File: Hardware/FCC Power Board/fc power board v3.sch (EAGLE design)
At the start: 40 parts

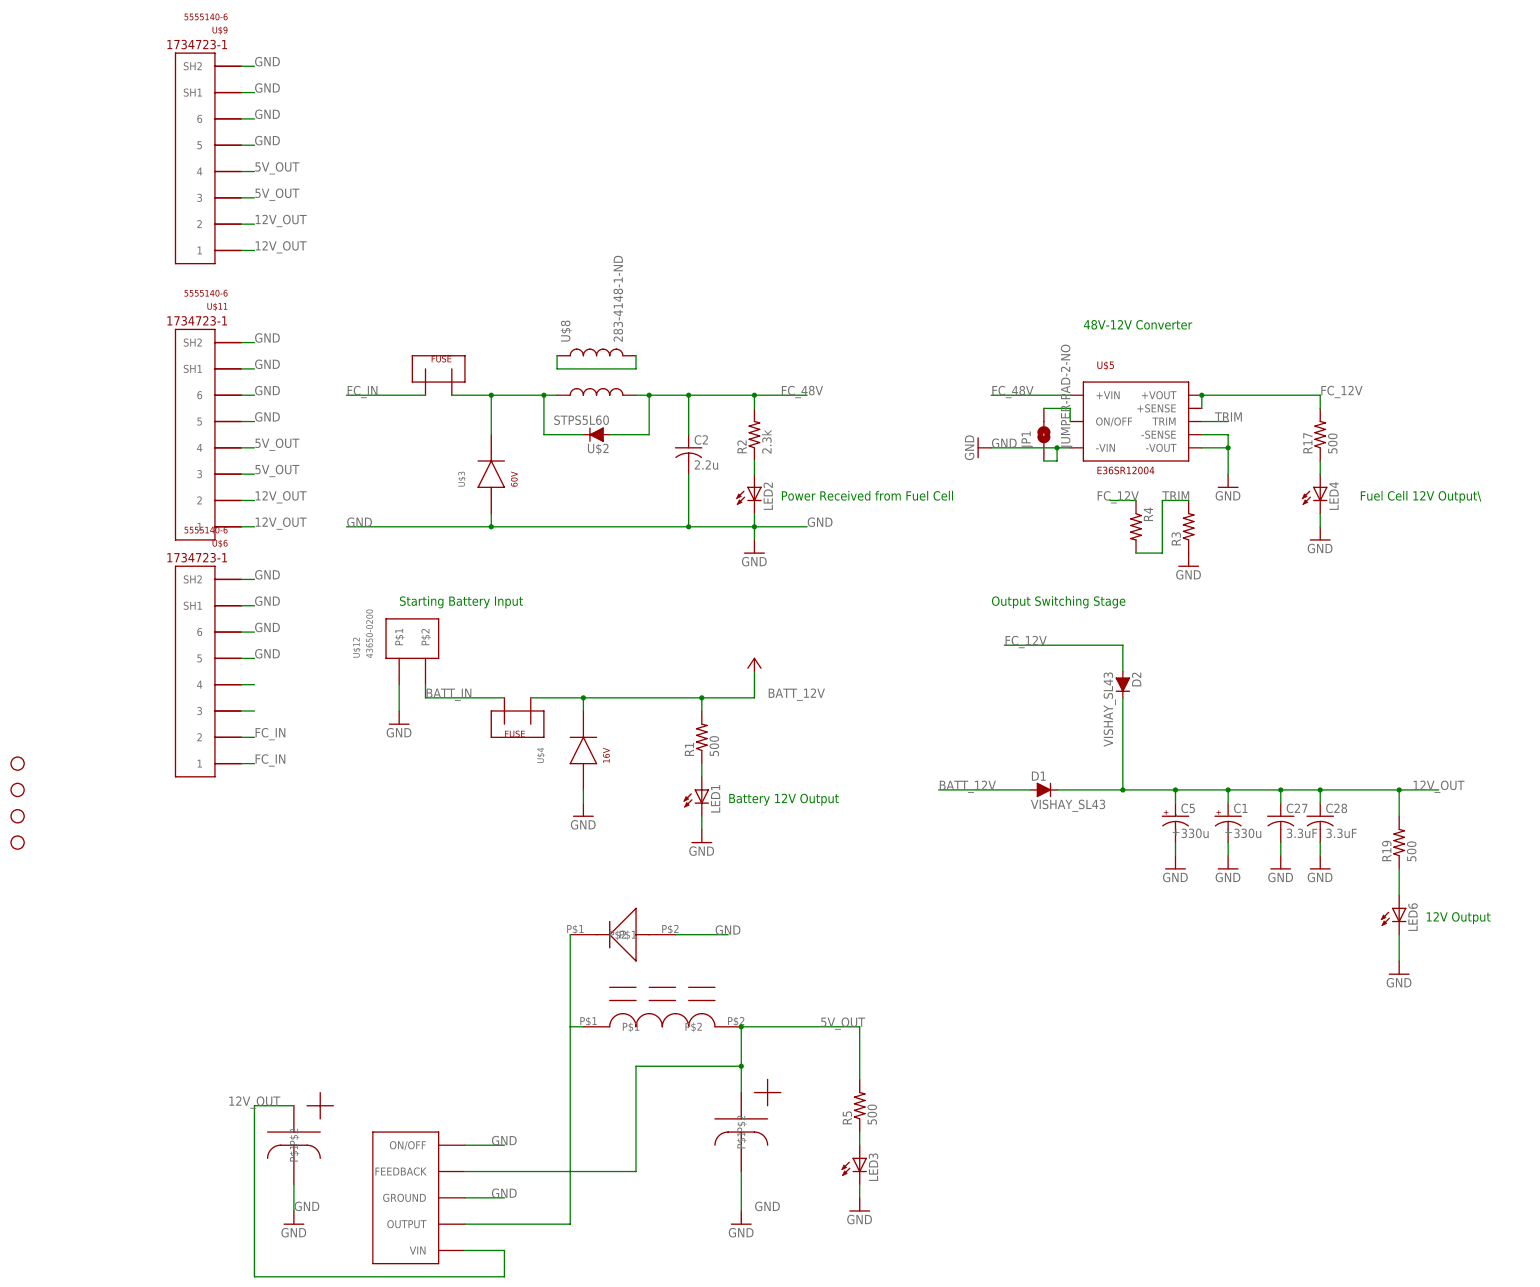
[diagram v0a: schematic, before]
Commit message: cleaned up fc power board silk screen
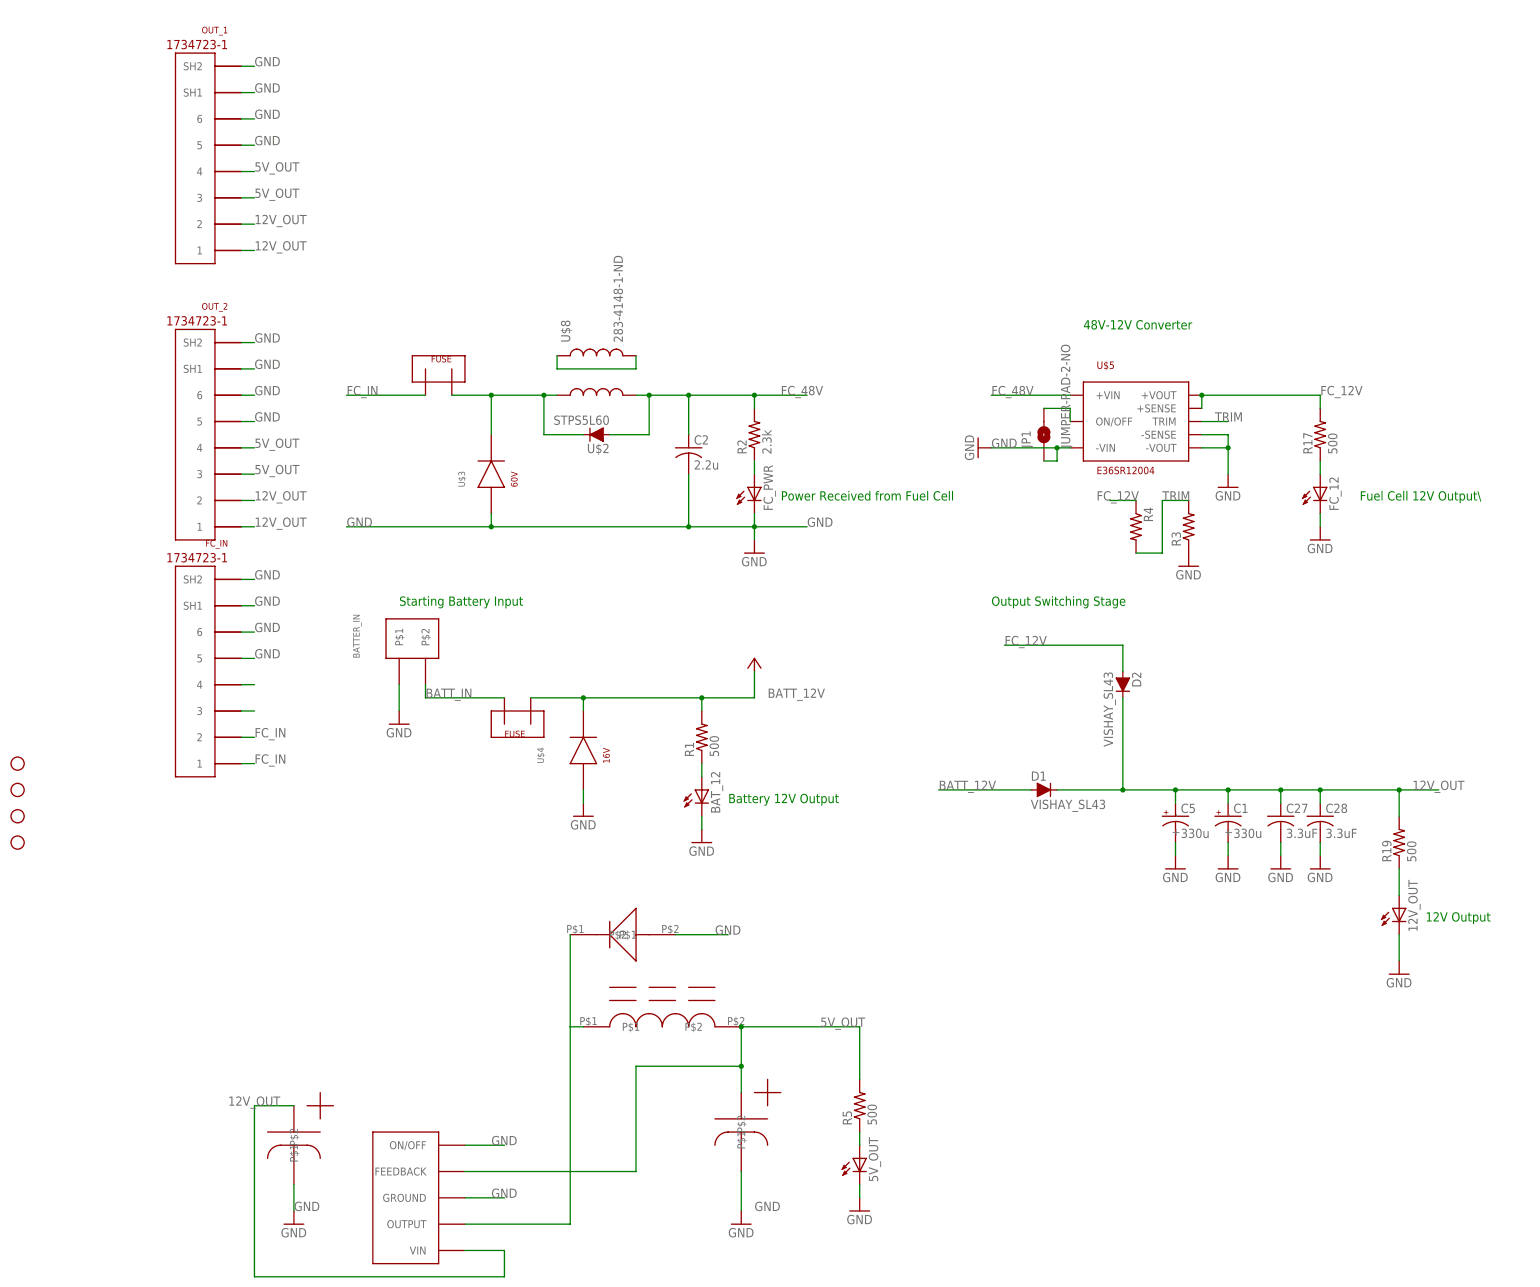
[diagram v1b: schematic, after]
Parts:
- renumbered LED1 to BAT_12, LED2 to FC_PWR, LED3 to 5V_OUT, LED4 to FC_12, LED6 to 12V_OUT, U$10 to BATTERY_FUSE, U$11 to OUT_2, U$12 to BATTER_IN, U$6 to FC_IN, U$9 to OUT_1

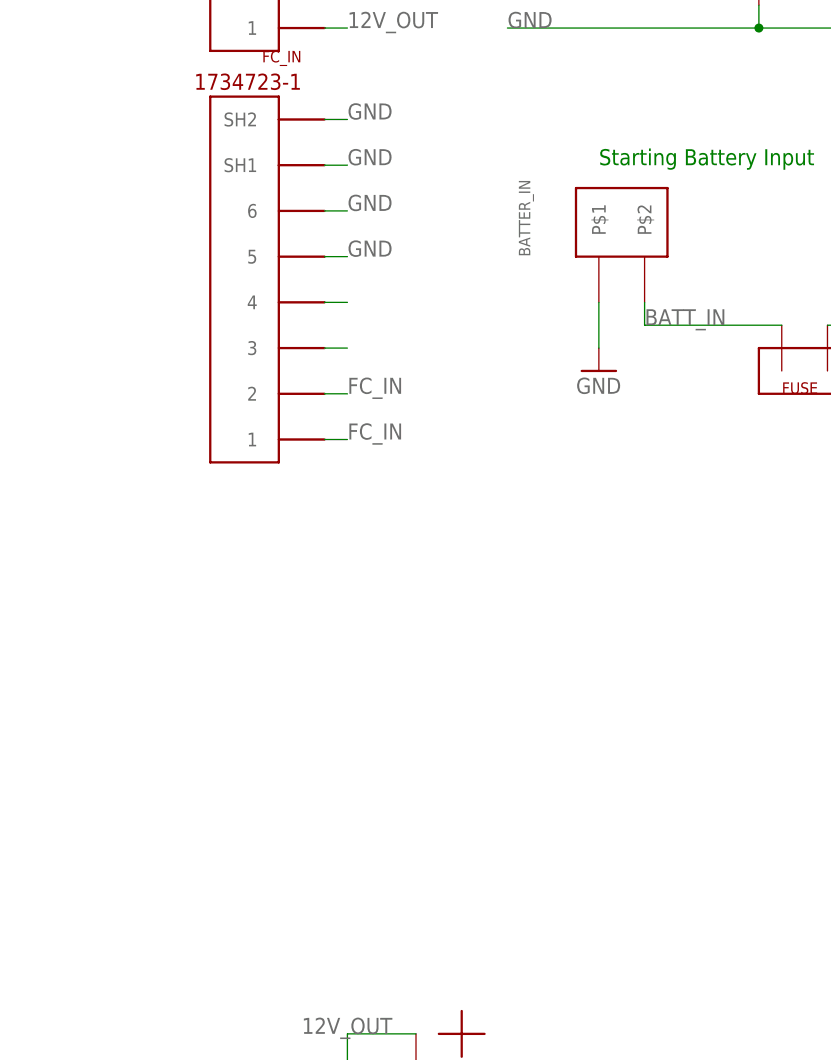
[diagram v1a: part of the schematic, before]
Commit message: FC power board updated
updated board gerbers generated
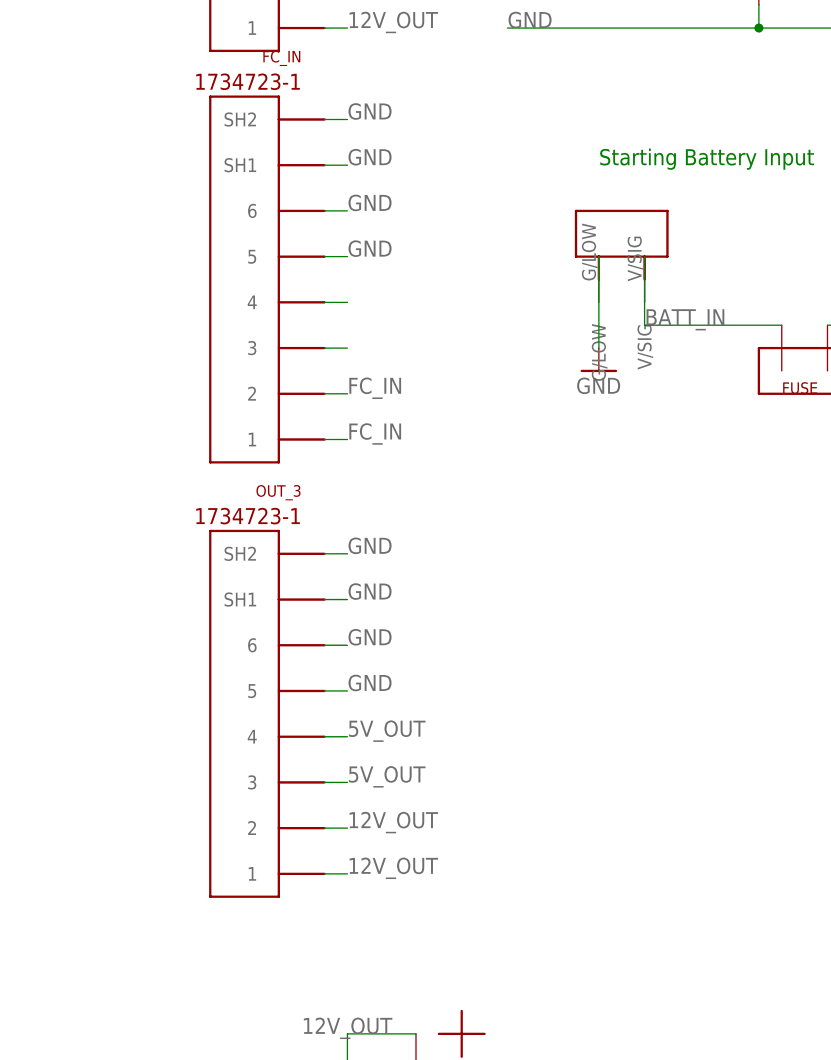
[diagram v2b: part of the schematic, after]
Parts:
- removed BATTER_IN: 43650-0200, Shell2013:43650-0200
- added OUT_3: 5555140-6, 5555140-6 RJ11:5555140-6
- added U$9: 2_PIN_TECONNECTOR, TE 2-pin connector:2_PIN_TECONNECTOR
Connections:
- net 12V_OUT: now also OUT_3.1, OUT_3.2
- net 5V_OUT: now also OUT_3.3, OUT_3.4
- net BATT_IN: now also U$9.V/SIG; no longer BATTER_IN.P$2
- net GND: now also OUT_3.5, OUT_3.6, OUT_3.SH1, OUT_3.SH2, U$9.G/LOW; no longer BATTER_IN.P$1
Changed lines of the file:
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@@
 <?xml version="1.0" encoding="utf-8"?>
 <!DOCTYPE eagle SYSTEM "eagle.dtd">
-<eagle version="8.1.0">
+<eagle version="8.6.1">
 <drawing>
 <settings>
 <setting alwaysvectorfont="no"/>
+<setting keepoldvectorfont="yes"/>
 <setting verticaltext="up"/>
 </settings>
@@
 <part name="PE36" library="supply1" deviceset="GND" device=""/>
 <part name="PE37" library="supply1" deviceset="GND" device=""/>
-<part name="BATTER_IN" library="Shell2013" deviceset="43650-0200" device="" value=""/>
 <part name="FC_12" library="SparkFun" deviceset="LED" device="1206"/>
 <part name="PE15" library="supply1" deviceset="GND" device=""/>
@@
 <part name="PE4" library="supply1" deviceset="GND" device=""/>
 <part name="JP1" library="SparkFun-Passives" deviceset="JUMPER-PAD-2-NO" device=""/>
+<part name="U$9" library="TE 2-pin connector" deviceset="2_PIN_TECONNECTOR" device=""/>
+<part name="OUT_3" library="5555140-6 RJ11" deviceset="5555140-6" device="" value=""/>
 </parts>
 <sheets>
@@
 <instance part="PE36" gate="1" x="76.2" y="-38.1"/>
 <instance part="PE37" gate="1" x="83.82" y="-38.1"/>
-<instance part="BATTER_IN" gate="G$1" x="-91.44" y="2.54" rot="R90"/>
 <instance part="FC_12" gate="G$1" x="83.82" y="35.56"/>
 <instance part="PE15" gate="1" x="83.82" y="25.4"/>
@@
 <instance part="PE4" gate="1" x="-114.3" y="-106.68"/>
 <instance part="JP1" gate="G$1" x="30.48" y="45.72" rot="R90"/>
+<instance part="U$9" gate="G$1" x="-91.44" y="7.62" rot="R90"/>
+<instance part="OUT_3" gate="G$1" x="-132.08" y="-53.34" rot="R180"/>
 </instances>
 <busses>
@@
 <label x="-121.92" y="81.28" size="1.778" layer="95"/>
 </segment>
+<segment>
+<pinref part="OUT_3" gate="G$1" pin="1"/>
+<wire x1="-124.46" y1="-66.04" x2="-121.92" y2="-66.04" width="0.1524" layer="91"/>
+<label x="-121.92" y="-66.04" size="1.778" layer="95"/>
+</segment>
+<segment>
+<pinref part="OUT_3" gate="G$1" pin="2"/>
+<wire x1="-124.46" y1="-60.96" x2="-121.92" y2="-60.96" width="0.1524" layer="91"/>
+<label x="-121.92" y="-60.96" size="1.778" layer="95"/>
+</segment>
 </net>
 <net name="GND" class="0">
@@
 <segment>
 <pinref part="GND2" gate="1" pin="GND"/>
-<pinref part="BATTER_IN" gate="G$1" pin="P$1"/>
-<wire x1="-93.98" y1="-7.62" x2="-93.98" y2="-2.54" width="0.1524" layer="91"/>
+<wire x1="-93.98" y1="-7.62" x2="-93.98" y2="2.54" width="0.1524" layer="91"/>
+<pinref part="U$9" gate="G$1" pin="G/LOW"/>
 </segment>
 <segment>
@@
 <wire x1="-5.08" y1="-99.06" x2="-5.08" y2="-101.6" width="0.1524" layer="91"/>
 </segment>
+<segment>
+<pinref part="OUT_3" gate="G$1" pin="SH2"/>
+<wire x1="-124.46" y1="-30.48" x2="-121.92" y2="-30.48" width="0.1524" layer="91"/>
+<label x="-121.92" y="-30.48" size="1.778" layer="95"/>
+</segment>
+<segment>
+<pinref part="OUT_3" gate="G$1" pin="SH1"/>
+<wire x1="-124.46" y1="-35.56" x2="-121.92" y2="-35.56" width="0.1524" layer="91"/>
+<label x="-121.92" y="-35.56" size="1.778" layer="95"/>
+</segment>
+<segment>
+<pinref part="OUT_3" gate="G$1" pin="5"/>
+<wire x1="-124.46" y1="-45.72" x2="-121.92" y2="-45.72" width="0.1524" layer="91"/>
+<label x="-121.92" y="-45.72" size="1.778" layer="95"/>
+</segment>
+<segment>
+<pinref part="OUT_3" gate="G$1" pin="6"/>
+<wire x1="-124.46" y1="-40.64" x2="-121.92" y2="-40.64" width="0.1524" layer="91"/>
+<label x="-121.92" y="-40.64" size="1.778" layer="95"/>
+</segment>
 </net>
 <net name="FC_12V" class="0">
@@
 <label x="-88.9" y="-5.08" size="1.778" layer="95"/>
 <pinref part="BATTERY_FUSE" gate="G$1" pin="IN"/>
-<wire x1="-88.9" y1="-2.54" x2="-88.9" y2="-5.08" width="0.1524" layer="91"/>
+<wire x1="-88.9" y1="2.54" x2="-88.9" y2="-5.08" width="0.1524" layer="91"/>
 <wire x1="-88.9" y1="-5.08" x2="-73.66" y2="-5.08" width="0.1524" layer="91"/>
-<pinref part="BATTER_IN" gate="G$1" pin="P$2"/>
+<pinref part="U$9" gate="G$1" pin="V/SIG"/>
 </segment>
 </net>
@@
 <label x="-12.7" y="-68.58" size="1.778" layer="95"/>
 </segment>
-</net>
+<segment>
+<pinref part="OUT_3" gate="G$1" pin="3"/>
+<wire x1="-124.46" y1="-55.88" x2="-121.92" y2="-55.88" width="0.1524" layer="91"/>
+<label x="-121.92" y="-55.88" size="1.778" layer="95"/>
+</segment>
+<segment>
+<pinref part="OUT_3" gate="G$1" pin="4"/>
+<wire x1="-124.46" y1="-50.8" x2="-121.92" y2="-50.8" width="0.1524" layer="91"/>
+<label x="-121.92" y="-50.8" size="1.778" layer="95"/>
+</segment>
+</net>
